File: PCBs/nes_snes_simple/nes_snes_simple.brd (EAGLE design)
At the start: 100 x 80 mm, 23 parts, among them IC1 74245

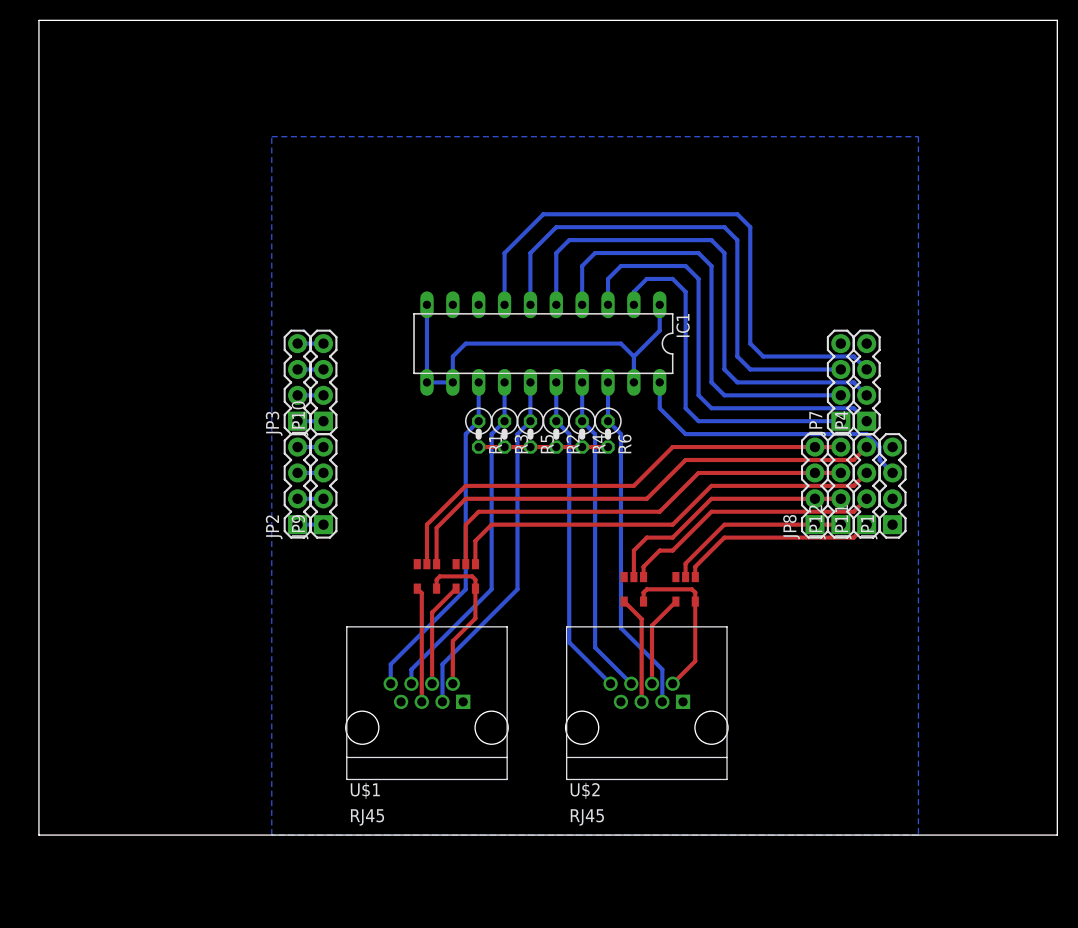
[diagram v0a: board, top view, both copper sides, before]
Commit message: Cleaned up the routing and board layout
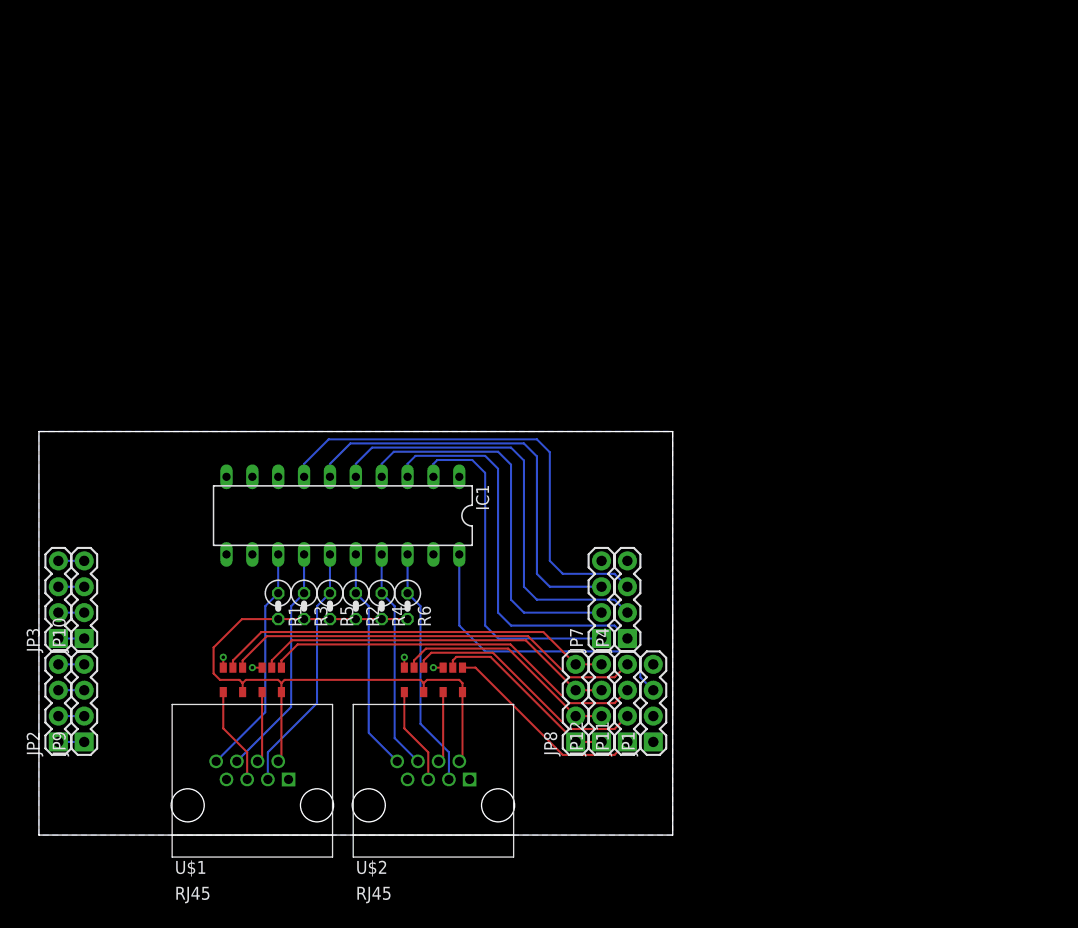
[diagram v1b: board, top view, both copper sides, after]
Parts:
- moved JP10 31.7 mm to (4.45, 19.3)
- moved JP11 31.7 mm to (57.8, 9.14)
- moved JP4 31.7 mm to (57.8, 19.3)
- moved JP8 31.7 mm to (52.7, 9.14)
- moved JP12 31.7 mm to (55.2, 9.14)
- moved JP2 31.7 mm to (1.91, 9.14)
- moved JP3 31.7 mm to (1.91, 19.3)
- moved JP7 31.7 mm to (55.2, 19.3)
- moved JP9 31.7 mm to (4.45, 9.14)
- moved JP1 31.7 mm to (60.3, 9.14)
- moved IC1 25.9 mm to (29.8, 31.4)
- moved R1 25.9 mm to (23.5, 22.5)
- moved R2 25.9 mm to (31.1, 22.5)
- moved R3 25.9 mm to (26.0, 22.5)
- moved R4 25.9 mm to (33.7, 22.5)
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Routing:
- net GND: track 40.2 -> 3.95 mm, vias 0 -> 4
- net CONSOLE+5V: track 44.9 -> 65.8 mm
- net P1_IODATA: track 34.9 -> 24.6 mm
- net P1_CLOCK: track 33.2 -> 22.8 mm
- net P1_LATCH: track 33.4 -> 23.1 mm
- net P2_CLOCK: track 31.8 -> 22.0 mm
- net P2_LATCH: track 31.6 -> 21.8 mm
- net P2_IODATA: track 33.6 -> 23.8 mm
- net P1_CLOCK_LV: track 55.2 -> 46.3 mm
- net P1_D1_LV: track 47.7 -> 39.4 mm
- net P1_LATCH_LV: track 49.1 -> 41.4 mm
- net P1_D1_OE_LV: track 49.1 -> 41.7 mm
- net P1_D0_LV: track 42.8 -> 35.9 mm
- net P1_IODATA_LV: track 49.1 -> 42.6 mm
- net P1_D0_OE_LV: track 43.5 -> 38.2 mm
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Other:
- board size 100 x 80 mm -> 62.2 x 39.6 mm

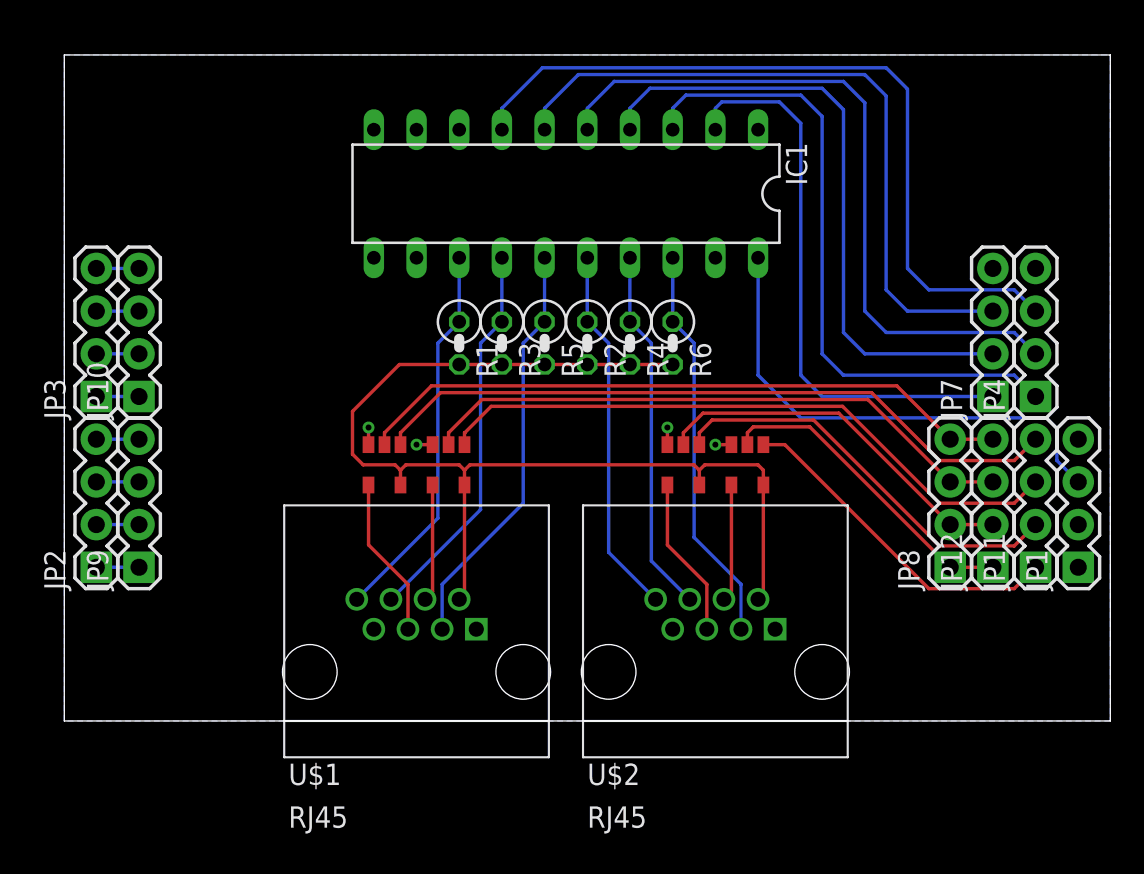
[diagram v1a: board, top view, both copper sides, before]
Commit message: Added a tap for all the 5v lines from the console. Fixed part labels. Added more labeling. Added a logo. Cleaned up the schematic.
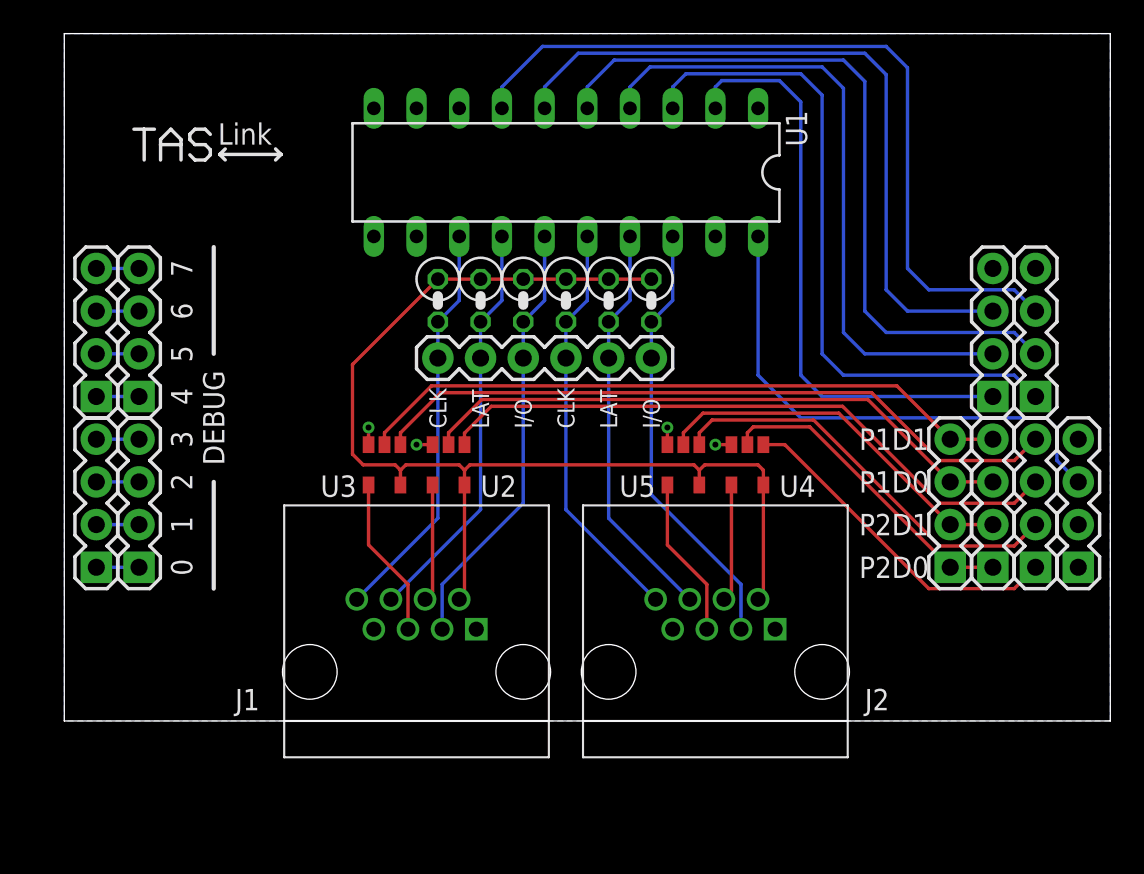
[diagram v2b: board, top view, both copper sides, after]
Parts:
- removed IC1: 74245, TASLink:DIL20
- added JP5: (no value), SparkFun-Connectors:1X06
- added U1: 74245, TASLink:DIL20
- moved R4 2.84 mm to (32.4, 25.0)
- moved R6 2.84 mm to (34.9, 25.0)
- moved R1 2.84 mm to (22.2, 25.0)
- moved R2 2.84 mm to (29.8, 25.0)
- moved R3 2.84 mm to (24.8, 25.0)
- moved R5 2.84 mm to (27.3, 25.0)
- renumbered U$1 to J1, U$2 to J2, U$3 to U2, U$4 to U4, U$5 to U3, U$6 to U5
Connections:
- net +3V3: now also U1.20; no longer IC1.20
- net CONSOLE+5V: now also R1.1, R2.1, R3.1, R4.1, R5.1, R6.1; no longer R1.2, R2.2, R3.2, R4.2, R5.2, R6.2
- net GND: now also U1.1, U1.10, U1.11, U1.12, U1.19; no longer IC1.1, IC1.10, IC1.11, IC1.12, IC1.19
- net P1_CLOCK: now also JP5.1, R1.2, U1.13; no longer IC1.13, R1.1
- net P1_CLOCK_LV: now also U1.7; no longer IC1.7
- net P1_IODATA: now also JP5.3, R5.2, U1.15; no longer IC1.15, R5.1
- net P1_IODATA_LV: now also U1.5; no longer IC1.5
- net P1_LATCH: now also JP5.2, R3.2, U1.14; no longer IC1.14, R3.1
- net P1_LATCH_LV: now also U1.6; no longer IC1.6
- net P2_CLOCK: now also JP5.4, R2.2, U1.16; no longer IC1.16, R2.1
- net P2_CLOCK_LV: now also U1.4; no longer IC1.4
- net P2_IODATA: now also JP5.6, R6.2, U1.18; no longer IC1.18, R6.1
- net P2_IODATA_LV: now also U1.2; no longer IC1.2
- net P2_LATCH: now also JP5.5, R4.2, U1.17; no longer IC1.17, R4.1
- net P2_LATCH_LV: now also U1.3; no longer IC1.3
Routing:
- net CONSOLE+5V: track 65.8 -> 68.2 mm
- net P2_LATCH: track 21.8 -> 24.1 mm
- net P2_IODATA: track 23.8 -> 26.1 mm
- net P2_CLOCK: track 22.0 -> 24.3 mm
- net P2_IODATA_LV: track 34.0 -> 35.2 mm
- net P2_CLOCK_LV: track 37.7 -> 38.9 mm
- net P1_LATCH_LV: track 41.4 -> 42.6 mm
- net P1_IODATA_LV: track 42.6 -> 43.8 mm
- net P2_LATCH_LV: track 38.9 -> 40.2 mm
- net P1_LATCH: track 23.1 -> 24.3 mm
- net P1_IODATA: track 24.6 -> 25.9 mm
- net P1_CLOCK: track 22.8 -> 24.1 mm
- net +3V3: track 29.8 -> 31.1 mm
- net P1_CLOCK_LV: track 46.3 -> 47.5 mm
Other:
- board size 62.2 x 39.6 mm -> 62.2 x 40.9 mm
- board text added: "0"
- board text added: "1"
- board text added: "2"
- board text added: "3"
- board text added: "4"
- board text added: "5"
- board text added: "6"
- board text added: "7"
- board text added: "CLK"
- board text added: "DEBUG"
- board text added: "I/O"
- board text added: "LAT"
- board text added: "Link"
- board text added: "P1D0"
- board text added: "P1D1"
- board text added: "P2D0"
- board text added: "P2D1"
